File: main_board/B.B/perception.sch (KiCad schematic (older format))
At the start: 10 parts

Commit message: preparation_to_drawing_PCB
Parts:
- added R?: 220, symbol Device:R
- added R? (x3): 220, Resistor_SMD:R_0402_1005Metric, symbol Device:R
- U?: footprint (none) -> Package_DFN_QFN:QFN-16-1EP_3x3mm_P0.5mm_EP1.7x1.7mm; LCSC (none) -> C113207
- U?: footprint (none) -> BB:SMD-8_2x2.5x0.65P; LCSC (none) -> C233787
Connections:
- net SCL: now also R?.2, R?.2; no longer U?.10 (SCL), U?.4 (SCK)
- net SDA: now also R?.2, R?.2; no longer U?.3 (SDA), U?.9 (SDA)
- new net: R?.1, U?.10 (SCL)
- new net: R?.1, U?.9 (SDA)
- new net: R?.1, U?.3 (SDA)
- new net: R?.1, U?.4 (SCK)
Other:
- moved on the sheet: C?, D?, R?
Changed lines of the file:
@@
 F 0 "U?" H 5625 3975 50  0000 C CNN
 F 1 "M41T62" H 5625 3884 50  0000 C CNN
-F 2 "" H 5600 3750 50  0001 C CNN
-F 3 "" H 5600 3750 50  0001 C CNN
+F 2 "Package_DFN_QFN:QFN-16-1EP_3x3mm_P0.5mm_EP1.7x1.7mm" H 5600 3750 50  0001 C CNN
+F 3 "https://datasheet.lcsc.com/szlcsc/STMicroelectronics-M41T62Q6F_C113207.pdf" H 5600 3750 50  0001 C CNN
+F 4 "C113207" H 5600 3750 50  0001 C CNN "LCSC"
 	1    5600 3750
 	1    0    0    -1
 $EndComp
-Text HLabel 4050 3650 1    50   Input ~ 0
+Text HLabel 4000 3650 1    50   Input ~ 0
 3V3
 $Comp
 L Device:D D?
 U 1 1 5F93AF19
-P 4300 3750
+P 4200 3750
 AR Path="/5F96CFDA/5F93AF19" Ref="D?"  Part="1"
 AR Path="/5F9EE529/5F9F24D4/5F93AF19" Ref="D?"  Part="1"
 AR Path="/5FA9DBB3/5F9F24D4/5F93AF19" Ref="D?"  Part="1"
-F 0 "D?" V 4346 3670 50  0000 R CNN
-F 1 "D" V 4255 3670 50  0000 R CNN
-F 2 "BB:SOD-323" H 4300 3750 50  0001 C CNN
-F 3 "https://datasheet.lcsc.com/szlcsc/SK-SD103AWS_C109204.pdf" H 4300 3750 50  0001 C CNN
-F 4 "C109204" V 4300 3750 50  0001 C CNN "LCSC"
-	1    4300 3750
+F 0 "D?" V 4246 3670 50  0000 R CNN
+F 1 "D" V 4155 3670 50  0000 R CNN
+F 2 "BB:SOD-323" H 4200 3750 50  0001 C CNN
+F 3 "https://datasheet.lcsc.com/szlcsc/SK-SD103AWS_C109204.pdf" H 4200 3750 50  0001 C CNN
+F 4 "C109204" V 4200 3750 50  0001 C CNN "LCSC"
+	1    4200 3750
 	-1   0    0    1
 $EndComp
 Wire Wire Line
-	4150 3750 4050 3750
-Wire Wire Line
-	4050 3750 4050 3650
+	4050 3750 4000 3750
+Wire Wire Line
+	4000 3750 4000 3650
 $Comp
 L Device:Crystal Y?
@@
 Wire Wire Line
 	6250 4450 6250 4400
-Text HLabel 5200 4050 0    50   Input ~ 0
-SDA
-Text HLabel 5200 4150 0    50   Input ~ 0
-SCL
 $Comp
 L B.B-eagle-import:GND #GND?
@@
 L B.B-eagle-import:GND #GND?
 U 1 1 5F94A059
-P 4700 4200
+P 4450 4200
 AR Path="/5F96CFDA/5F94A059" Ref="#GND?"  Part="1"
 AR Path="/5F9EE529/5F9F24D4/5F94A059" Ref="#GND?"  Part="1"
 AR Path="/5FA9DBB3/5F9F24D4/5F94A059" Ref="#GND?"  Part="1"
-F 0 "#GND?" H 4700 4200 50  0001 C CNN
-F 1 "GND" H 4700 4120 59  0000 C CNN
-F 2 "" H 4700 4200 50  0001 C CNN
-F 3 "" H 4700 4200 50  0001 C CNN
-	1    4700 4200
-	1    0    0    -1
-$EndComp
-Wire Wire Line
-	4700 3800 4700 3750
+F 0 "#GND?" H 4450 4200 50  0001 C CNN
+F 1 "GND" H 4450 4120 59  0000 C CNN
+F 2 "" H 4450 4200 50  0001 C CNN
+F 3 "" H 4450 4200 50  0001 C CNN
+	1    4450 4200
+	1    0    0    -1
+$EndComp
+Wire Wire Line
+	4450 3800 4450 3750
 $Comp
 L B.B-eagle-import:NC #NC?
@@
 F 0 "U?" H 5600 5375 50  0000 C CNN
 F 1 "SPL06" H 5600 5284 50  0000 C CNN
-F 2 "" H 5600 5150 50  0001 C CNN
-F 3 "" H 5600 5150 50  0001 C CNN
+F 2 "BB:SMD-8_2x2.5x0.65P" H 5600 5150 50  0001 C CNN
+F 3 "https://datasheet.lcsc.com/szlcsc/1907081118_Goertek-SPL06-007_C233787.pdf" H 5600 5150 50  0001 C CNN
+F 4 "C233787" H 5600 5150 50  0001 C CNN "LCSC"
 	1    5600 5150
 	1    0    0    -1
 $EndComp
-Text HLabel 5200 5550 0    50   Input ~ 0
+Text HLabel 4900 5550 0    50   Input ~ 0
 SCL
-Text HLabel 5200 5450 0    50   Input ~ 0
+Text HLabel 4900 5450 0    50   Input ~ 0
 SDA
-Connection ~ 6450 5250
-Wire Wire Line
-	6450 5250 6600 5250
-Text HLabel 6600 5250 2    50   Input ~ 0
+Text HLabel 6450 5250 2    50   Input ~ 0
 int_baro
 $Comp
@@
 	-1   0    0    1
 $EndComp
-Text HLabel 4050 5050 1    50   Input ~ 0
+Text HLabel 4400 5100 1    50   Input ~ 0
 3V3
-Wire Wire Line
-	4050 5050 4050 5150
-Wire Wire Line
-	4050 5150 4700 5150
 $Comp
 L Device:C C?
 U 1 1 5F975C33
-P 4700 5350
+P 4400 5350
 AR Path="/5F96CFDA/5F975C33" Ref="C?"  Part="1"
 AR Path="/5F9EE529/5F9F24D4/5F975C33" Ref="C?"  Part="1"
 AR Path="/5FA9DBB3/5F9F24D4/5F975C33" Ref="C?"  Part="1"
-F 0 "C?" H 4815 5396 50  0000 L CNN
-F 1 "1uf" H 4815 5305 50  0000 L CNN
-F 2 "Resistor_SMD:R_0402_1005Metric" H 4738 5200 50  0001 C CNN
-F 3 "~" H 4700 5350 50  0001 C CNN
-F 4 "C52923" H 4700 5350 50  0001 C CNN "LCSC"
-	1    4700 5350
+F 0 "C?" H 4515 5396 50  0000 L CNN
+F 1 "1uf" H 4515 5305 50  0000 L CNN
+F 2 "Resistor_SMD:R_0402_1005Metric" H 4438 5200 50  0001 C CNN
+F 3 "~" H 4400 5350 50  0001 C CNN
+F 4 "C52923" H 4400 5350 50  0001 C CNN "LCSC"
+	1    4400 5350
 	1    0    0    -1
 $EndComp
@@
 L B.B-eagle-import:GND #GND?
 U 1 1 5F975C39
-P 4700 5600
+P 4400 5600
 AR Path="/5F96CFDA/5F975C39" Ref="#GND?"  Part="1"
 AR Path="/5F9EE529/5F9F24D4/5F975C39" Ref="#GND?"  Part="1"
 AR Path="/5FA9DBB3/5F9F24D4/5F975C39" Ref="#GND?"  Part="1"
-F 0 "#GND?" H 4700 5600 50  0001 C CNN
-F 1 "GND" H 4700 5520 59  0000 C CNN
-F 2 "" H 4700 5600 50  0001 C CNN
-F 3 "" H 4700 5600 50  0001 C CNN
-	1    4700 5600
-	1    0    0    -1
-$EndComp
-Wire Wire Line
-	4700 5200 4700 5150
+F 0 "#GND?" H 4400 5600 50  0001 C CNN
+F 1 "GND" H 4400 5520 59  0000 C CNN
+F 2 "" H 4400 5600 50  0001 C CNN
+F 3 "" H 4400 5600 50  0001 C CNN
+	1    4400 5600
+	1    0    0    -1
+$EndComp
+Wire Wire Line
+	4400 5200 4400 5150
 $Comp
 L Device:C C?
 U 1 1 5F9780C8
-P 4700 3950
+P 4450 3950
 AR Path="/5F96CFDA/5F9780C8" Ref="C?"  Part="1"
 AR Path="/5F9EE529/5F9F24D4/5F9780C8" Ref="C?"  Part="1"
 AR Path="/5FA9DBB3/5F9F24D4/5F9780C8" Ref="C?"  Part="1"
-F 0 "C?" H 4815 3996 50  0000 L CNN
-F 1 "1uf" H 4815 3905 50  0000 L CNN
-F 2 "Resistor_SMD:R_0402_1005Metric" H 4738 3800 50  0001 C CNN
-F 3 "~" H 4700 3950 50  0001 C CNN
-F 4 "C52923" H 4700 3950 50  0001 C CNN "LCSC"
-	1    4700 3950
-	1    0    0    -1
-$EndComp
-Connection ~ 4700 5150
-Wire Wire Line
-	4700 5150 5150 5150
-Connection ~ 4700 3750
-Wire Wire Line
-	4700 3750 5200 3750
-Wire Wire Line
-	4450 3750 4700 3750
+F 0 "C?" H 4565 3996 50  0000 L CNN
+F 1 "1uf" H 4565 3905 50  0000 L CNN
+F 2 "Resistor_SMD:R_0402_1005Metric" H 4488 3800 50  0001 C CNN
+F 3 "~" H 4450 3950 50  0001 C CNN
+F 4 "C52923" H 4450 3950 50  0001 C CNN "LCSC"
+	1    4450 3950
+	1    0    0    -1
+$EndComp
+Connection ~ 4400 5150
+Wire Wire Line
+	4400 5150 5150 5150
+Connection ~ 4450 3750
+Wire Wire Line
+	4450 3750 5200 3750
+Wire Wire Line
+	4350 3750 4450 3750
 Wire Wire Line
 	5200 5250 5150 5250
 Wire Wire Line
 	5150 5250 5150 5150
-Connection ~ 5150 5150
 Wire Wire Line
 	5150 5150 5200 5150
 Wire Wire Line
-	6000 5250 6450 5250
+	6000 5250 6350 5250
 $Comp
 L B.B-eagle-import:GND #GND?
@@
 L Device:R R?
 U 1 1 5F990B4D
-P 6450 5450
+P 6350 5450
 AR Path="/5F96CFDA/5F990B4D" Ref="R?"  Part="1"
 AR Path="/5F9EE529/5F9F24D4/5F990B4D" Ref="R?"  Part="1"
 AR Path="/5FA9DBB3/5F9F24D4/5F990B4D" Ref="R?"  Part="1"
-F 0 "R?" H 6520 5496 50  0000 L CNN
-F 1 "100k" H 6520 5405 50  0000 L CNN
-F 2 "Resistor_SMD:R_0402_1005Metric" V 6380 5450 50  0001 C CNN
-F 3 "~" H 6450 5450 50  0001 C CNN
-F 4 "C25741" H 6450 5450 50  0001 C CNN "LCSC"
-	1    6450 5450
-	1    0    0    -1
-$EndComp
-Wire Wire Line
-	6450 5300 6450 5250
+F 0 "R?" H 6420 5496 50  0000 L CNN
+F 1 "100k" H 6420 5405 50  0000 L CNN
+F 2 "Resistor_SMD:R_0402_1005Metric" V 6280 5450 50  0001 C CNN
+F 3 "~" H 6350 5450 50  0001 C CNN
+F 4 "C25741" H 6350 5450 50  0001 C CNN "LCSC"
+	1    6350 5450
+	1    0    0    -1
+$EndComp
+Wire Wire Line
+	6350 5300 6350 5250
 $Comp
 L B.B-eagle-import:GND #GND?
 U 1 1 5F9924A7
-P 6450 5700
+P 6350 5700
 AR Path="/5F96CFDA/5F9924A7" Ref="#GND?"  Part="1"
 AR Path="/5F9EE529/5F9F24D4/5F9924A7" Ref="#GND?"  Part="1"
 AR Path="/5FA9DBB3/5F9F24D4/5F9924A7" Ref="#GND?"  Part="1"
-F 0 "#GND?" H 6450 5700 50  0001 C CNN
-F 1 "GND" H 6450 5620 59  0000 C CNN
-F 2 "" H 6450 5700 50  0001 C CNN
-F 3 "" H 6450 5700 50  0001 C CNN
-	1    6450 5700
-	1    0    0    -1
-$EndComp
+F 0 "#GND?" H 6350 5700 50  0001 C CNN
+F 1 "GND" H 6350 5620 59  0000 C CNN
+F 2 "" H 6350 5700 50  0001 C CNN
+F 3 "" H 6350 5700 50  0001 C CNN
+	1    6350 5700
+	1    0    0    -1
+$EndComp
+$Comp
+L Device:R R?
+U 1 1 5FAFDE55
+P 5050 5450
+AR Path="/5FA3274C/5FAFDE55" Ref="R?"  Part="1"
+AR Path="/5F9EE529/5FAFDE55" Ref="R?"  Part="1"
+AR Path="/5F9EE529/5F9F24D4/5FAFDE55" Ref="R?"  Part="1"
+F 0 "R?" V 4950 5550 50  0000 C CNN
+F 1 "220" V 4950 5350 50  0000 C CNN
+F 2 "" V 4980 5450 50  0001 C CNN
+F 3 "~" H 5050 5450 50  0001 C CNN
+F 4 "C25092" V 5050 5450 50  0001 C CNN "LCSC"
+	1    5050 5450
+	0    1    1    0
+$EndComp
+$Comp
+L Device:R R?
+U 1 1 5FAFE429
+P 5050 5550
+AR Path="/5FA3274C/5FAFE429" Ref="R?"  Part="1"
+AR Path="/5F9EE529/5FAFE429" Ref="R?"  Part="1"
+AR Path="/5F9EE529/5F9F24D4/5FAFE429" Ref="R?"  Part="1"
+F 0 "R?" V 5150 5650 50  0000 C CNN
+F 1 "220" V 5150 5450 50  0000 C CNN
+F 2 "Resistor_SMD:R_0402_1005Metric" V 4980 5550 50  0001 C CNN
+F 3 "~" H 5050 5550 50  0001 C CNN
+F 4 "C25092" V 5050 5550 50  0001 C CNN "LCSC"
+	1    5050 5550
+	0    1    1    0
+$EndComp
+Connection ~ 5150 5150
+Text HLabel 4900 4150 0    50   Input ~ 0
+SCL
+Text HLabel 4900 4050 0    50   Input ~ 0
+SDA
+$Comp
+L Device:R R?
+U 1 1 5FB01470
+P 5050 4050
+AR Path="/5FA3274C/5FB01470" Ref="R?"  Part="1"
+AR Path="/5F9EE529/5FB01470" Ref="R?"  Part="1"
+AR Path="/5F9EE529/5F9F24D4/5FB01470" Ref="R?"  Part="1"
+F 0 "R?" V 4950 4150 50  0000 C CNN
+F 1 "220" V 4950 3950 50  0000 C CNN
+F 2 "Resistor_SMD:R_0402_1005Metric" V 4980 4050 50  0001 C CNN
+F 3 "~" H 5050 4050 50  0001 C CNN
+F 4 "C25092" V 5050 4050 50  0001 C CNN "LCSC"
+	1    5050 4050
+	0    1    1    0
+$EndComp
+$Comp
+L Device:R R?
+U 1 1 5FB01477
+P 5050 4150
+AR Path="/5FA3274C/5FB01477" Ref="R?"  Part="1"
+AR Path="/5F9EE529/5FB01477" Ref="R?"  Part="1"
+AR Path="/5F9EE529/5F9F24D4/5FB01477" Ref="R?"  Part="1"
+F 0 "R?" V 5150 4250 50  0000 C CNN
+F 1 "220" V 5150 4050 50  0000 C CNN
+F 2 "Resistor_SMD:R_0402_1005Metric" V 4980 4150 50  0001 C CNN
+F 3 "~" H 5050 4150 50  0001 C CNN
+F 4 "C25092" V 5050 4150 50  0001 C CNN "LCSC"
+	1    5050 4150
+	0    1    1    0
+$EndComp
+Wire Wire Line
+	4400 5100 4400 5150
+Connection ~ 6350 5250
+Wire Wire Line
+	6350 5250 6450 5250
 $EndSCHEMATC

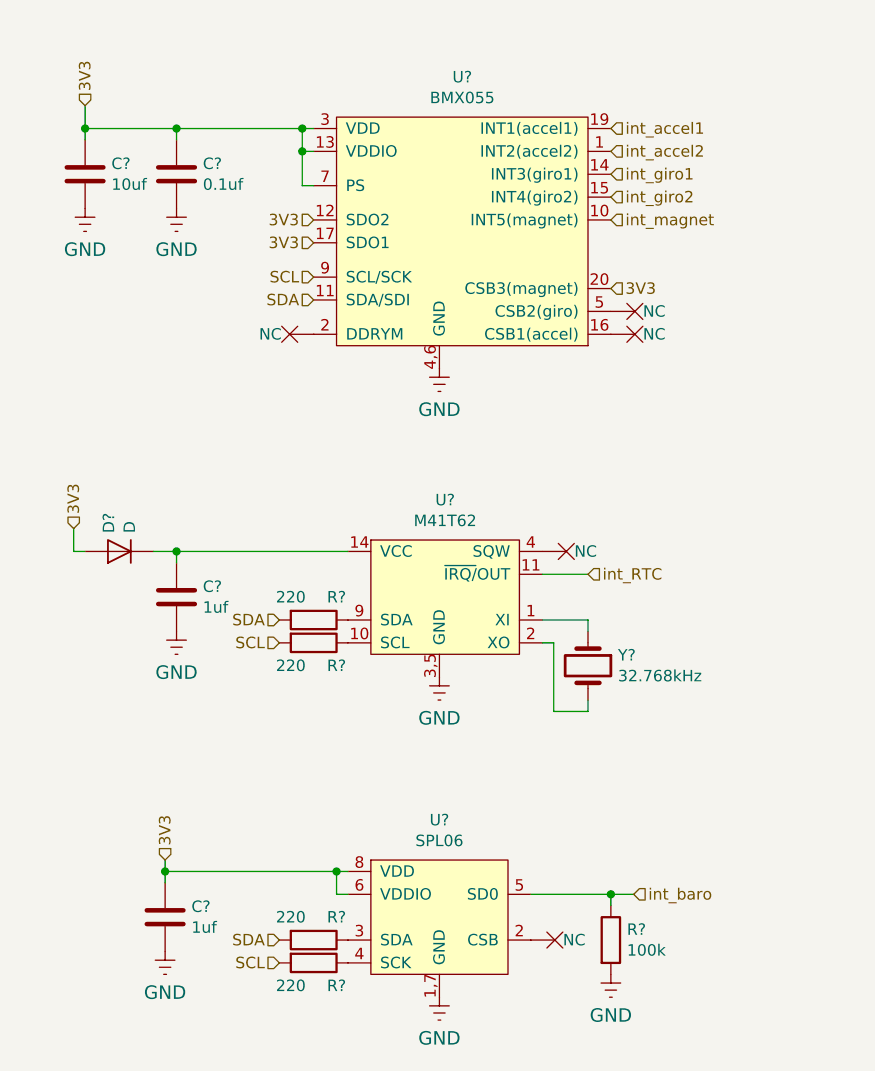
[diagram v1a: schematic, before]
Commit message: complete_preparation_to_drawing_PCB
footprint for all component and LCSC code for everything for mounting in JLCPCB
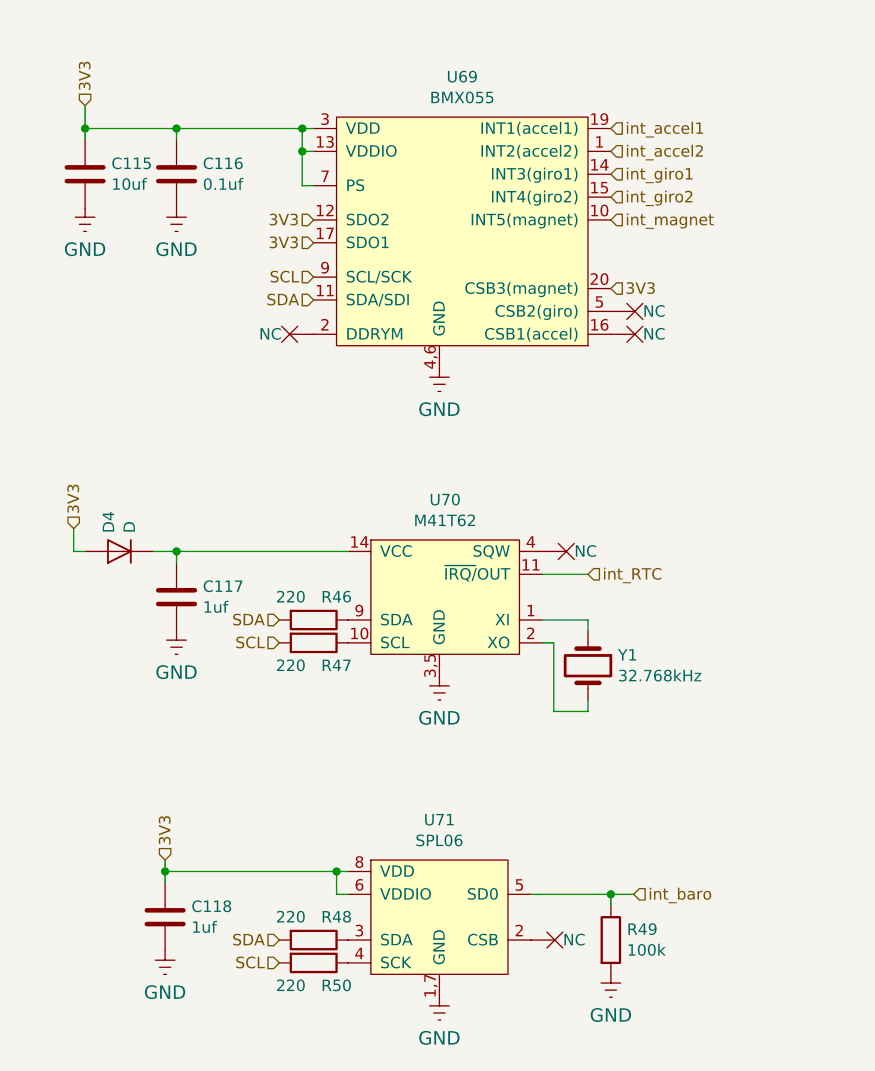
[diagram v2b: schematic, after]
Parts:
- removed R?: 220, symbol Device:R
- removed R?: 220, Resistor_SMD:R_0402_1005Metric, symbol Device:R
- added R48, R50: 220, Resistor_SMD:R_0402_1005Metric, symbol Device:R
- gave numbers to parts that had none: 12
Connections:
- net SCL: now also R50.2
- net SDA: now also R48.2
- net at U71.3 (SDA): now also R48.1
- net at U71.4 (SCK): now also R50.1

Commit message: optimalizace_kondenzatoru
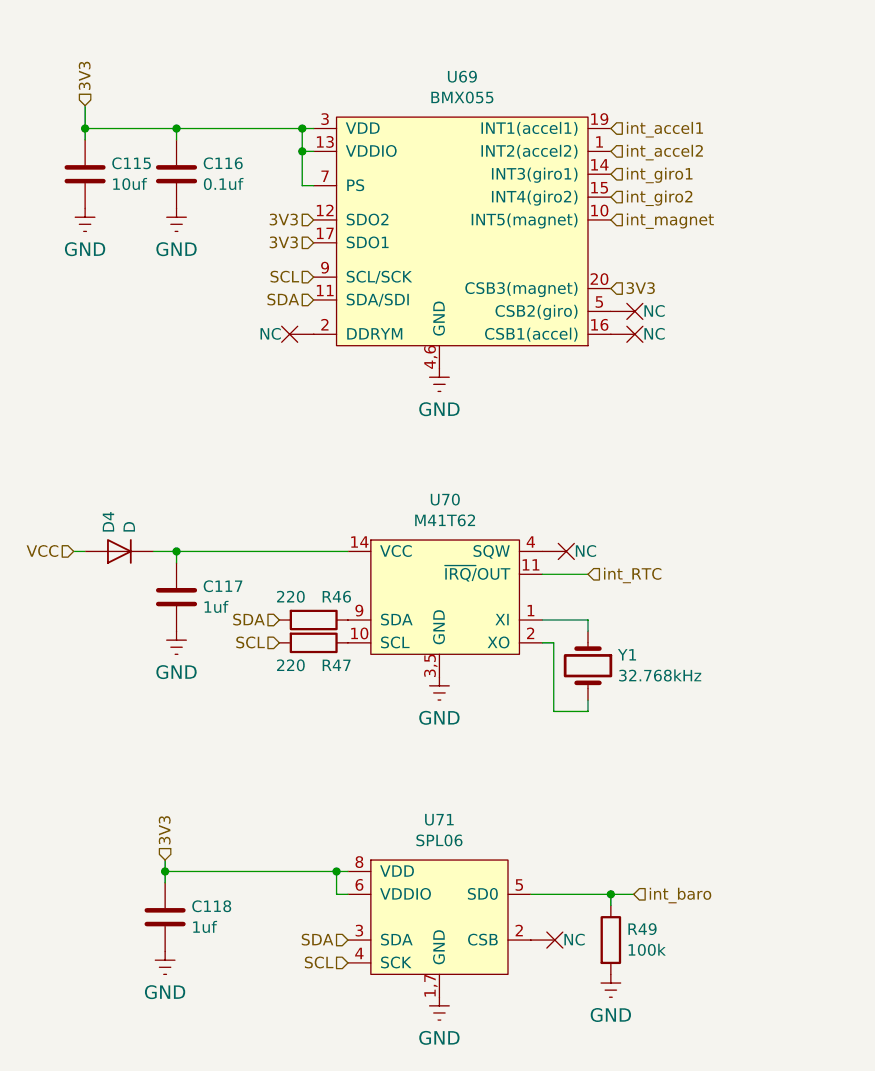
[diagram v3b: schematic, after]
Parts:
- removed R48, R50: 220, Resistor_SMD:R_0402_1005Metric, symbol Device:R
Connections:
- net 3V3: no longer D4.2 (A)
- net SCL: now also U71.4 (SCK)
- net SDA: now also U71.3 (SDA)
- new net VCC: D4.2 (A)
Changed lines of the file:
@@
 	1    0    0    -1
 $EndComp
-Text HLabel 4000 3650 1    50   Input ~ 0
-3V3
 $Comp
 L Device:D D?
@@
 Wire Wire Line
 	4050 3750 4000 3750
-Wire Wire Line
-	4000 3750 4000 3650
 $Comp
 L Device:Crystal Y?
@@
 	1    0    0    -1
 $EndComp
-Text HLabel 4900 5550 0    50   Input ~ 0
+Text HLabel 5200 5550 0    50   Input ~ 0
 SCL
-Text HLabel 4900 5450 0    50   Input ~ 0
+Text HLabel 5200 5450 0    50   Input ~ 0
 SDA
 Text HLabel 6450 5250 2    50   Input ~ 0
@@
 Wire Wire Line
 	6350 5250 6450 5250
-$Comp
-L Device:R R?
-U 1 1 5FBC93C7
-P 5050 5450
-AR Path="/5FA3274C/5FBC93C7" Ref="R?"  Part="1"
-AR Path="/5F9EE529/5FBC93C7" Ref="R?"  Part="1"
-AR Path="/5F9EE529/5F9F24D4/5FBC93C7" Ref="R48"  Part="1"
-F 0 "R48" V 4950 5550 50  0000 C CNN
-F 1 "220" V 4950 5350 50  0000 C CNN
-F 2 "Resistor_SMD:R_0402_1005Metric" V 4980 5450 50  0001 C CNN
-F 3 "~" H 5050 5450 50  0001 C CNN
-F 4 "C25092" V 5050 5450 50  0001 C CNN "LCSC"
-	1    5050 5450
-	0    1    1    0
-$EndComp
-$Comp
-L Device:R R?
-U 1 1 5FBC93CE
-P 5050 5550
-AR Path="/5FA3274C/5FBC93CE" Ref="R?"  Part="1"
-AR Path="/5F9EE529/5FBC93CE" Ref="R?"  Part="1"
-AR Path="/5F9EE529/5F9F24D4/5FBC93CE" Ref="R50"  Part="1"
-F 0 "R50" V 5150 5650 50  0000 C CNN
-F 1 "220" V 5150 5450 50  0000 C CNN
-F 2 "Resistor_SMD:R_0402_1005Metric" V 4980 5550 50  0001 C CNN
-F 3 "~" H 5050 5550 50  0001 C CNN
-F 4 "C25092" V 5050 5550 50  0001 C CNN "LCSC"
-	1    5050 5550
-	0    1    1    0
-$EndComp
+Text HLabel 4000 3750 0    50   Input ~ 0
+VCC
 $EndSCHEMATC

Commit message: start vith pcb
firsxxt proposal component layout of main board
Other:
- moved on the sheet: C115, C116, C117, C118, D4, R46, R47, R49, U69, U70, U71, Y1

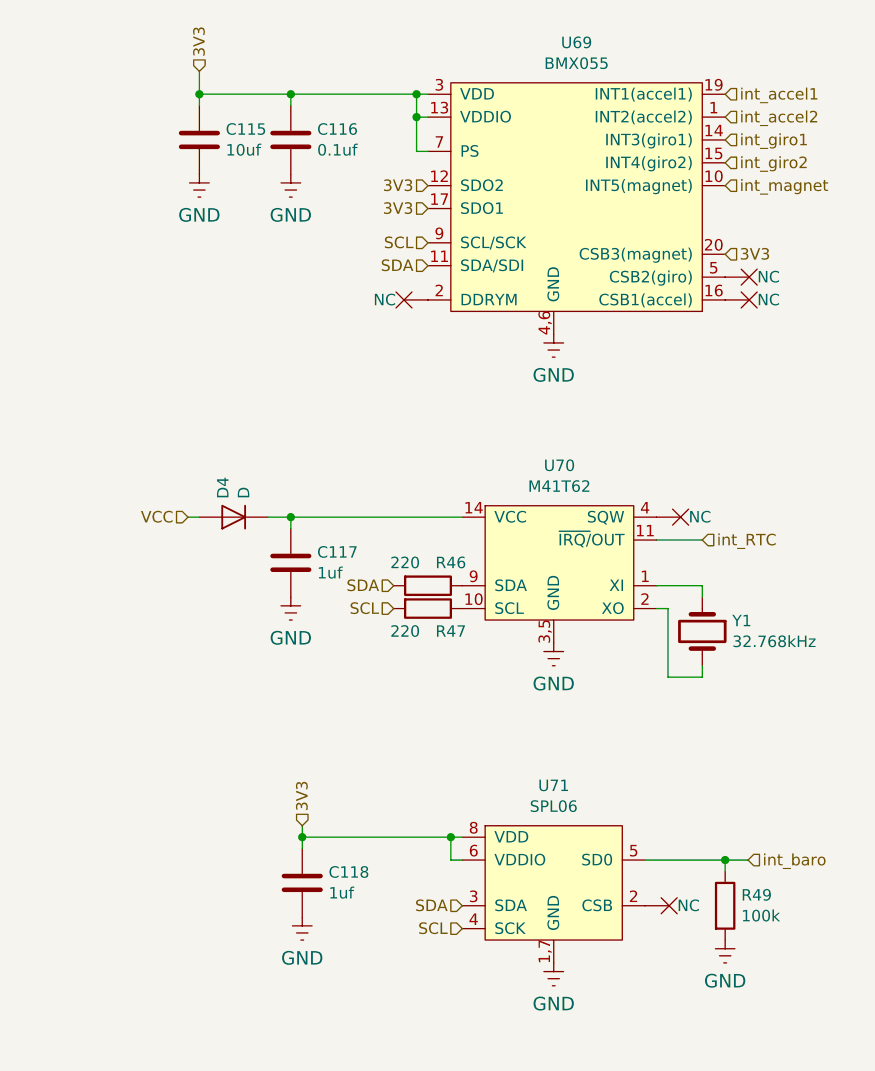
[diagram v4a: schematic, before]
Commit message: orezavani
smazaní A9G, SD karty, a zvuku
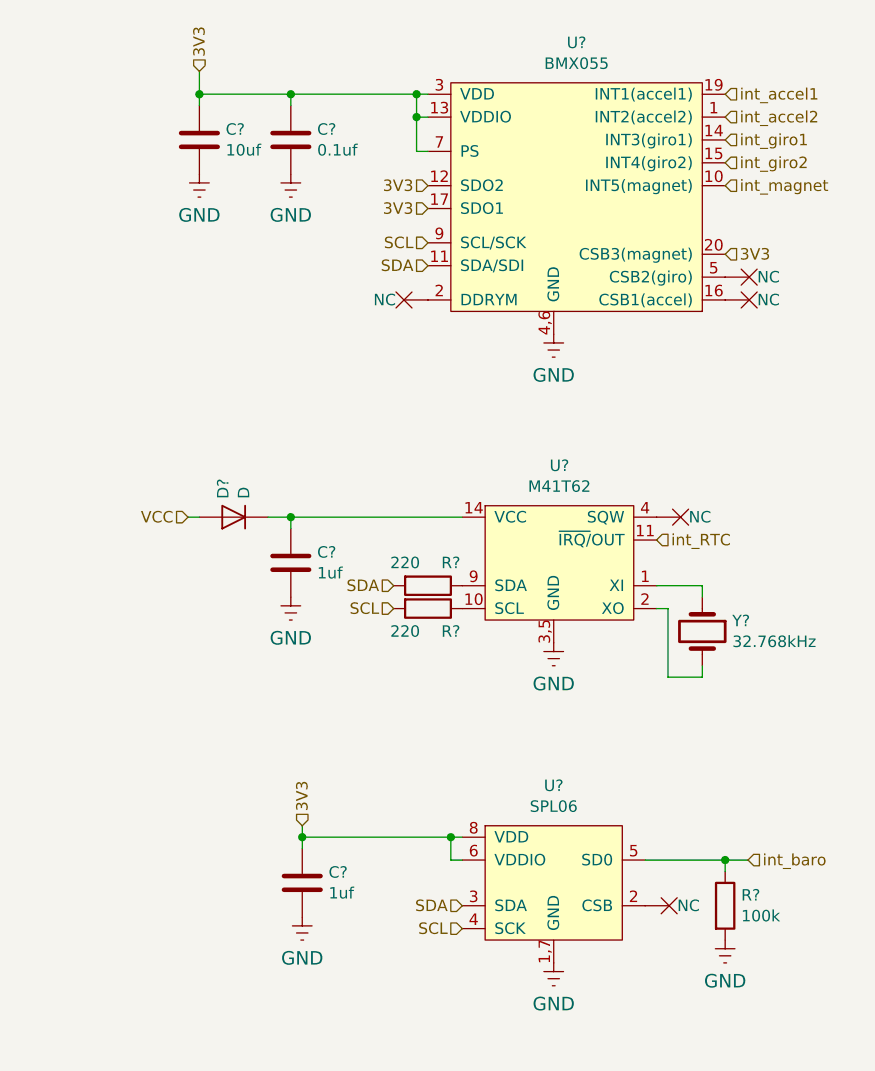
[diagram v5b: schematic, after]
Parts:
- Y1: LCSC (none) -> C156244; LSCS C156244 -> (none)
